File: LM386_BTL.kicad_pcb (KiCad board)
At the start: 2 copper layers, 44.5 x 44.5 mm, 31 parts, among them J1 IN, J2 L_OUT, J3 R_OUT, J4 POWER, U1 LM386, U2 LM386, U3 LM386, U4 LM386

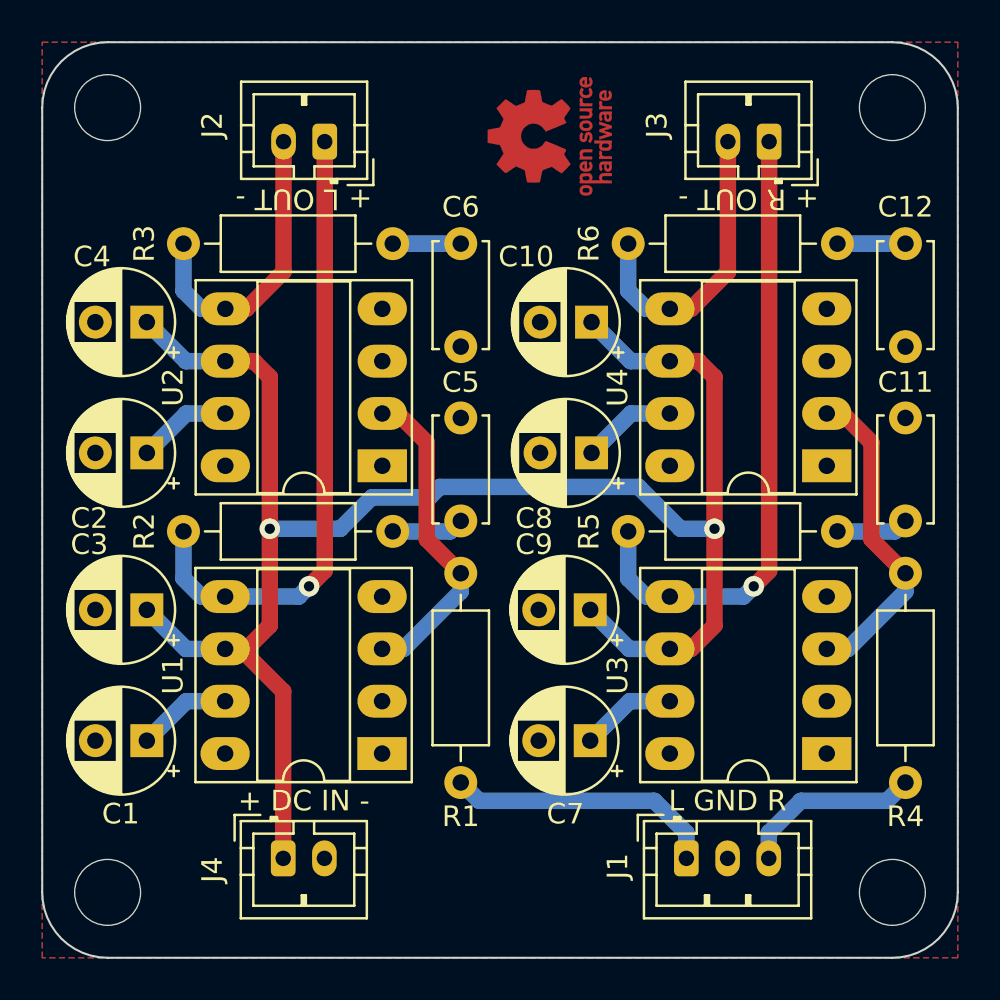
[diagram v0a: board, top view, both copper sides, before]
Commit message: Swap positive and negative amplifier position prevent from oscillation
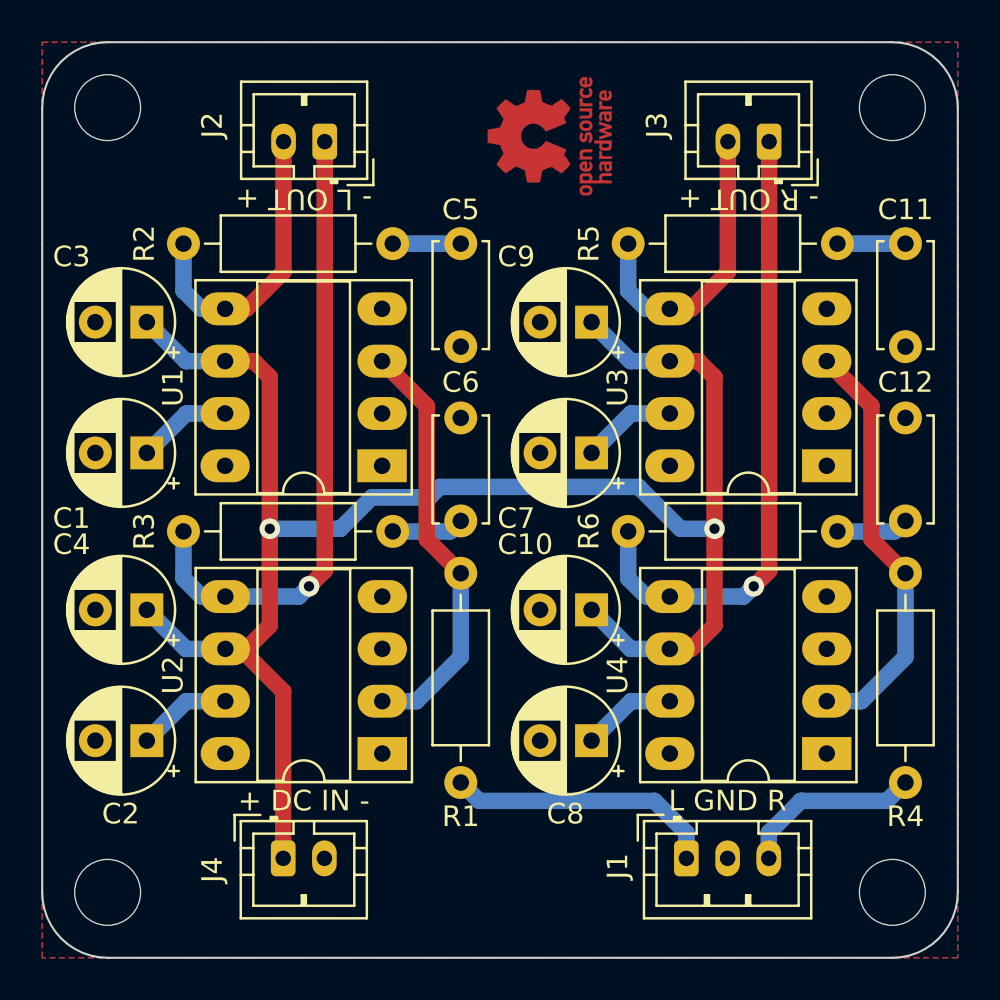
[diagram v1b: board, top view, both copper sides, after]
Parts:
- moved C9 14.0 mm to (26.7, 13.6)
- moved C7 14.0 mm to (26.7, 19.9)
- moved C10 14.0 mm to (26.7, 27.6)
- moved C3 14.0 mm to (5.08, 13.6)
- moved C4 14.0 mm to (5.08, 27.6)
- moved C1 14.0 mm to (5.08, 19.9)
- moved C2 14.0 mm to (5.08, 33.9)
- moved C8 14.0 mm to (26.7, 33.9)
- moved R2 14.0 mm to (6.86, 9.78)
- moved R3 14.0 mm to (6.86, 23.7)
- moved R5 14.0 mm to (28.4, 9.78)
- moved R6 14.0 mm to (28.4, 23.7)
- moved U1 14.0 mm to (16.5, 20.6)
- moved U2 14.0 mm to (16.5, 34.5)
- moved U3 14.0 mm to (38.1, 20.6)
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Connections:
- R2 pad 1: Net-(J2-Pad1) -> Net-(J2-Pad2)
- R3 pad 1: Net-(J2-Pad2) -> Net-(J2-Pad1)
- R5 pad 1: Net-(J3-Pad1) -> Net-(J3-Pad2)
- R6 pad 1: Net-(J3-Pad2) -> Net-(J3-Pad1)
- U1 pad 5: Net-(J2-Pad1) -> Net-(J2-Pad2)
- U2 pad 5: Net-(J2-Pad2) -> Net-(J2-Pad1)
- U3 pad 5: Net-(J3-Pad1) -> Net-(J3-Pad2)
- U4 pad 5: Net-(J3-Pad2) -> Net-(J3-Pad1)
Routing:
- net Net-(R4-Pad2): track 15.6 -> 20.7 mm
- net Net-(R1-Pad2): track 15.6 -> 20.6 mm
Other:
- board text added: "- L OUT +"
- board text added: "- R OUT +"
- board text added: "DANCHOUZHOU DEC 20, 2022 THE ULTIMATE LM386 BTL AMP"
- board text removed: "+ L OUT -"
- board text removed: "+ R OUT -"
- board text removed: "DANCHOUZHOU DEC 18, 2022 THE ULTIMATE LM386 BTL AMP"

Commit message: Swap output polarity
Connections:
- J2 pad 1: Net-(J2-Pad1) -> Net-(R2-Pad1)
- J2 pad 2: Net-(J2-Pad2) -> Net-(R3-Pad1)
- J3 pad 1: Net-(J3-Pad1) -> Net-(R5-Pad1)
- R2 pad 1: Net-(J2-Pad2) -> Net-(R2-Pad1)
- R3 pad 1: Net-(J2-Pad1) -> Net-(R3-Pad1)
- R5 pad 1: Net-(J3-Pad2) -> Net-(R5-Pad1)
- R6 pad 1: Net-(J3-Pad1) -> Net-(J3-Pad2)
- U1 pad 5: Net-(J2-Pad2) -> Net-(R2-Pad1)
- U2 pad 5: Net-(J2-Pad1) -> Net-(R3-Pad1)
- U3 pad 5: Net-(J3-Pad2) -> Net-(R5-Pad1)
- U4 pad 5: Net-(J3-Pad1) -> Net-(J3-Pad2)
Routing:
- net Net-(R3-Pad1): track 0.00 -> 31.1 mm, vias 0 -> 1
- net Net-(J2-Pad1): track 30.9 -> 0.00 mm, vias 1 -> 0
- net Net-(J3-Pad1): track 30.9 -> 0.00 mm, vias 1 -> 0
- net Net-(R2-Pad1): track 0.00 -> 16.9 mm
- net Net-(R5-Pad1): track 0.00 -> 16.9 mm
- net Net-(J3-Pad2): track 14.6 -> 31.1 mm, vias 0 -> 1
- net Net-(J2-Pad2): track 14.6 -> 0.00 mm
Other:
- board text added: "+ L OUT -"
- board text added: "+ R OUT -"
- board text added: "DANCHOUZHOU FEB 7, 2023 THE ULTIMATE LM386 BTL AMP"
- board text removed: "- L OUT +"
- board text removed: "- R OUT +"
- board text removed: "DANCHOUZHOU DEC 20, 2022 THE ULTIMATE LM386 BTL AMP"

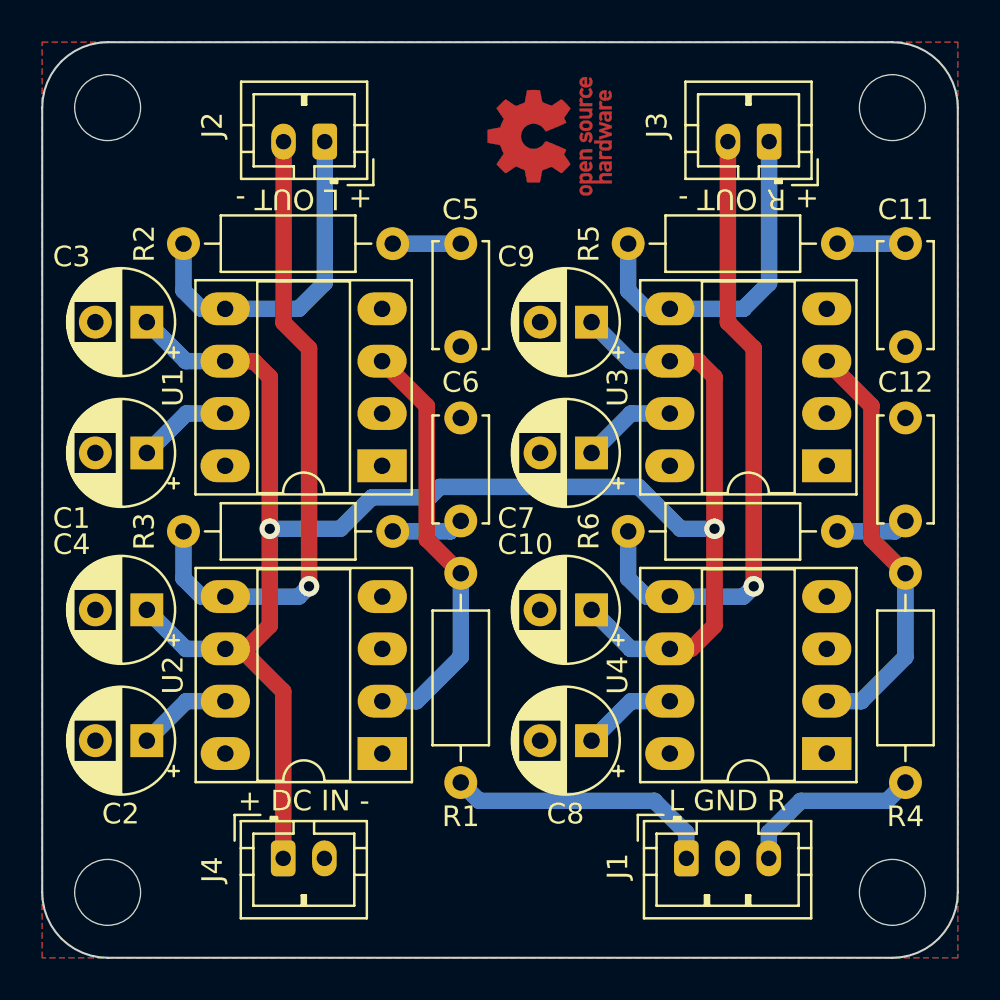
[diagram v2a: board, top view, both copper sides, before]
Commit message: Change capacitor footprint P2.50mm into P2.00mm
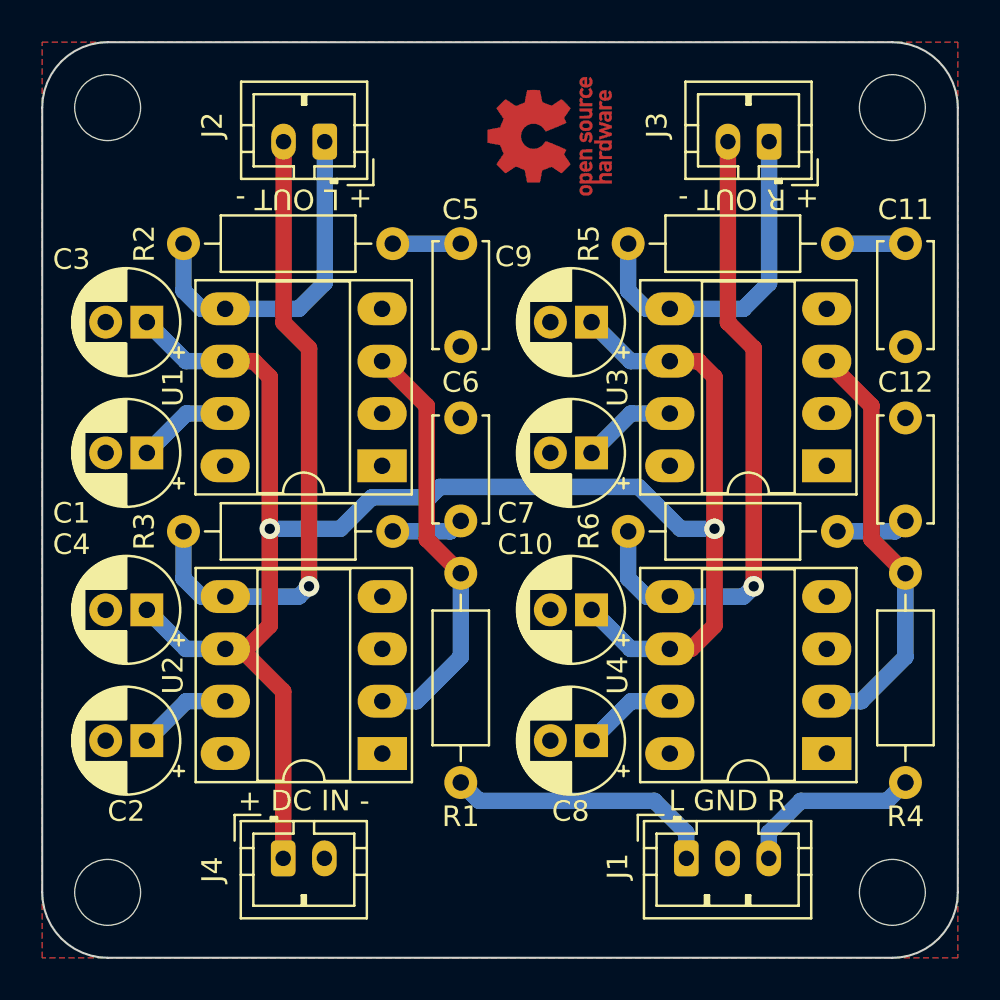
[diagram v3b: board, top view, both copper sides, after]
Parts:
- C1, C10, C2, C3, C4, C7, C8, C9: footprint Capacitor_THT:CP_Radial_D5.0mm_P2.50mm -> Capacitor_THT:CP_Radial_D5.0mm_P2.00mm
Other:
- board text added: "20231006: Change capacitor footprint P2.50mm into P2.00mm"
- board text added: "DANCHOUZHOU OCT 6, 2023 THE ULTIMATE LM386 BTL AMP"
- board text removed: "DANCHOUZHOU FEB 7, 2023 THE ULTIMATE LM386 BTL AMP"
